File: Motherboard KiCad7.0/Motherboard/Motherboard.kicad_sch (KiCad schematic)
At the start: 92 parts, among them J1 USB_B_Micro, J10 430450200, J11 430450200, J12 430450200, J2 SWD_01x04_Pin, J3 430450200, J4 430450200, J5 B04B-XASK-1, J6 430450200, J7 430450200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

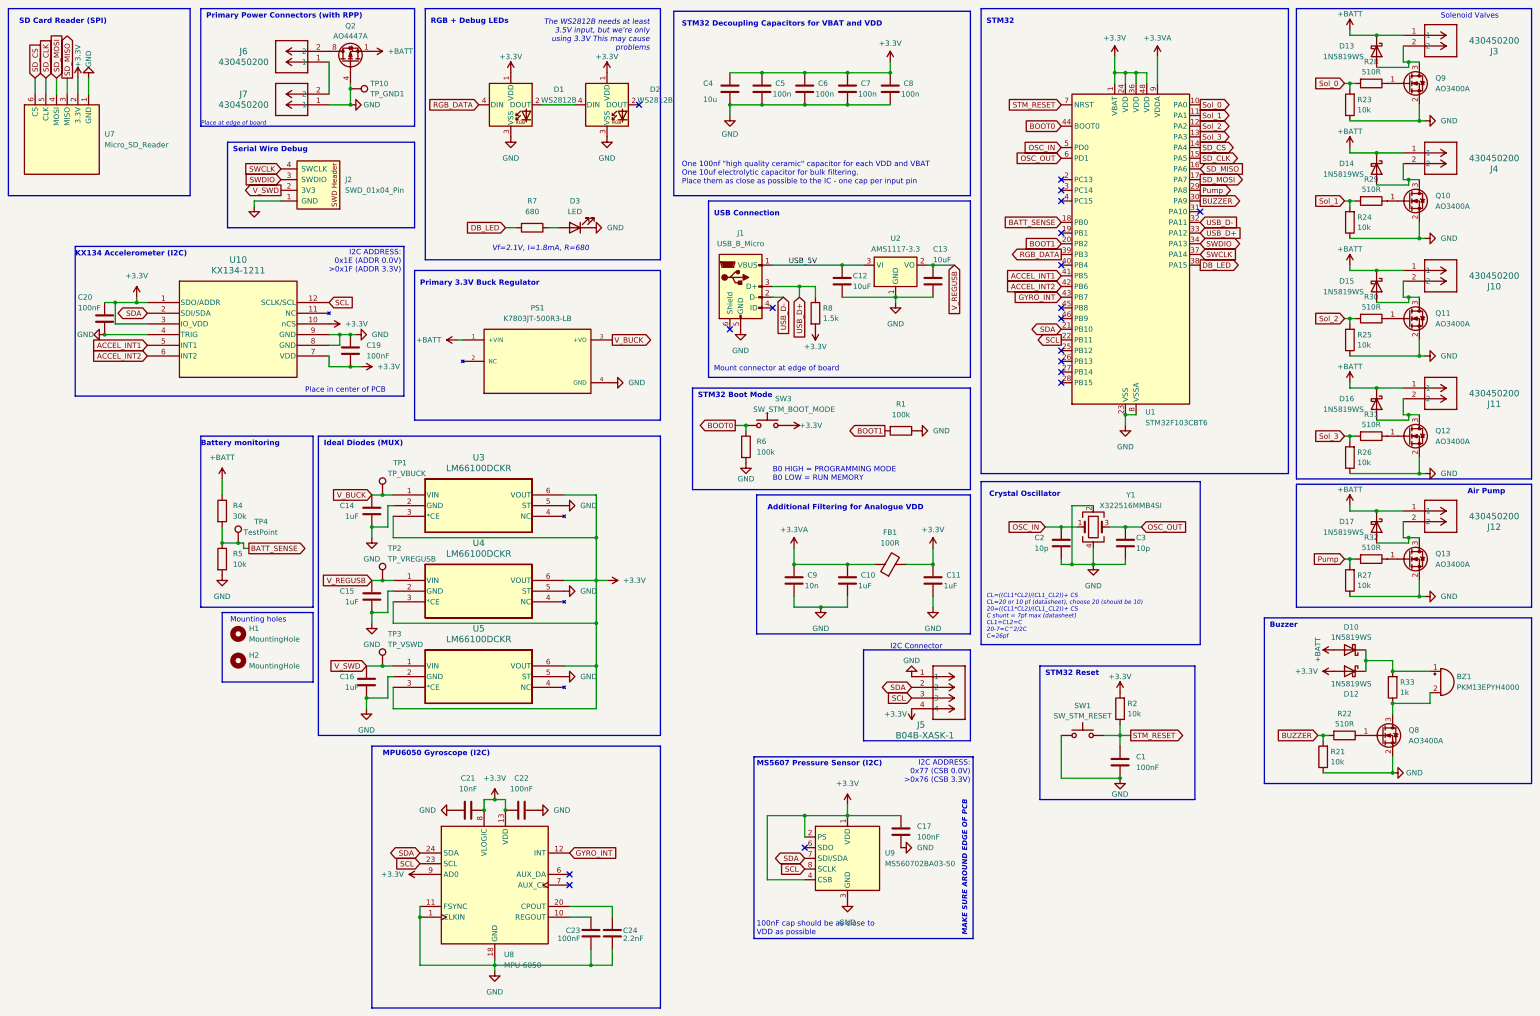
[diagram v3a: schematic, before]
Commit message: Schematic and layout changes
Rewired ADCs
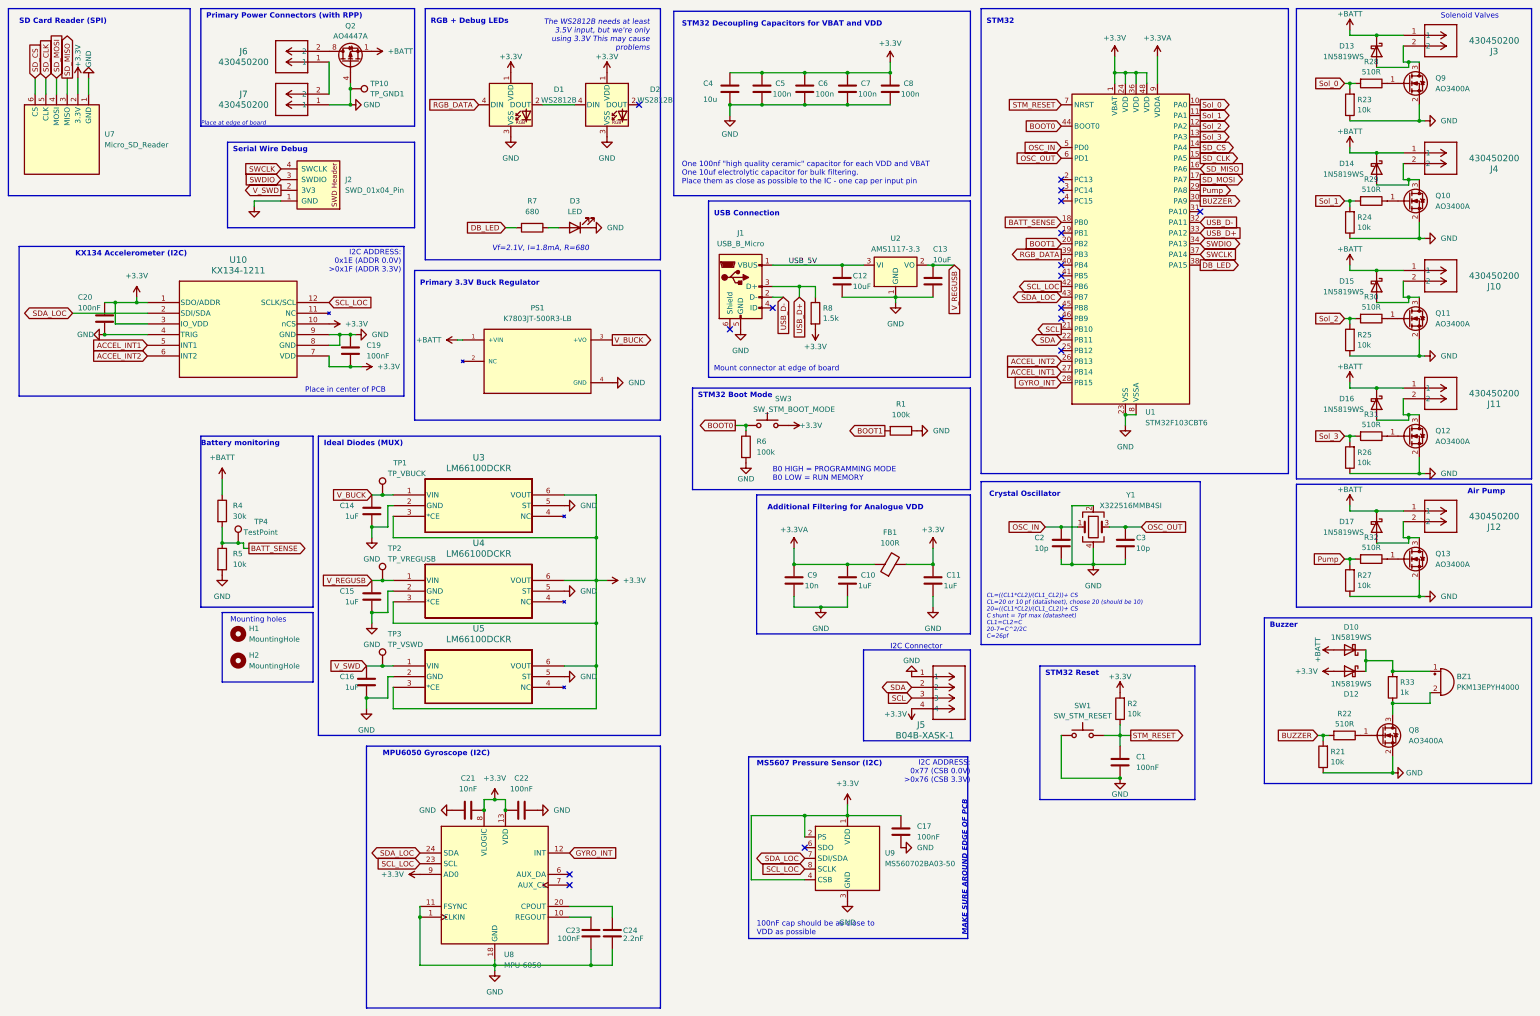
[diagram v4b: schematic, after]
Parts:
- J10, J11, J12, J4, J6, J7: footprint CON_430450200_MOL -> CONN 0430450200:CON_430450200_MOL
- J5: footprint CONN_B04B-XASK-1_JST -> B04B_XASK_1:CONN_B04B-XASK-1_JST
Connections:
- net ACCEL_INT1: now also U1.27 (PB14); no longer U1.41 (PB5)
- net ACCEL_INT2: now also U1.26 (PB13); no longer U1.42 (PB6)
- net GYRO_INT: now also U1.28 (PB15); no longer U1.43 (PB7)
- net SCL: now also U1.21 (PB10); no longer U1.22 (PB11), U10.12 (SCLK/SCL), U8.23 (SCL), U9.8 (SCLK)
- net SDA: now also U1.22 (PB11); no longer U1.21 (PB10), U10.2 (SDI/SDA), U8.24 (SDA), U9.7 (SDI/SDA)
- new net SCL_LOC: U1.42 (PB6), U10.12 (SCLK/SCL), U8.23 (SCL), U9.8 (SCLK)
- new net SDA_LOC: U1.43 (PB7), U10.2 (SDI/SDA), U8.24 (SDA), U9.7 (SDI/SDA)
- no-connect marks 18 -> 16
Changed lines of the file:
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@@
   (junction (at 388.62 71.12) (diameter 0) (color 0 0 0 0)
   )
-  (no_connect (at 303.53 102.87))
-  (no_connect (at 303.53 100.33))
   (no_connect (at 303.53 90.17))
   (no_connect (at 203.2 39.37))
   (no_connect (at 303.53 62.23))
   (no_connect (at 303.53 87.63))
+  (no_connect (at 303.53 80.01))
   (no_connect (at 303.53 77.47))
-  (no_connect (at 303.53 105.41))
   (no_connect (at 234.95 87.63))
   (no_connect (at 336.55 64.77))
@@
     (stroke (width 0) (type default))
   )
-  (wire (pts (xy 233.68 223.52) (xy 233.68 208.28))
+  (wire (pts (xy 229.87 223.52) (xy 229.87 208.28))
     (stroke (width 0) (type default))
   )
@@
     (stroke (width 0) (type default))
   )
-  (wire (pts (xy 233.68 208.28) (xy 242.57 208.28))
+  (wire (pts (xy 229.87 208.28) (xy 242.57 208.28))
     (stroke (width 0) (type default))
   )
@@
     (stroke (width 0) (type default))
   )
-  (wire (pts (xy 242.57 223.52) (xy 233.68 223.52))
+  (wire (pts (xy 242.57 223.52) (xy 229.87 223.52))
     (stroke (width 0) (type default))
   )
@@
     (stroke (width 0) (type default))
   )
+  (wire (pts (xy 68.58 88.9) (xy 86.36 88.9))
+    (stroke (width 0) (type default))
+  )
   (wire (pts (xy 372.11 106.68) (xy 378.46 106.68))
     (stroke (width 0) (type default))
@@
     (fill (type none))
   )
-  (rectangle (start 230.505 194.31) (end 282.575 237.49)
+  (rectangle (start 229.235 194.31) (end 281.305 237.49)
     (stroke (width 0) (type default))
     (fill (type none))
@@
     (fill (type none))
   )
-  (rectangle (start 69.215 73.025) (end 147.32 108.585)
+  (rectangle (start 55.88 73.025) (end 147.32 108.585)
     (stroke (width 0) (type default))
     (fill (type none))
@@
     (fill (type none))
   )
-  (rectangle (start 139.7 191.77) (end 208.28 254)
+  (rectangle (start 138.43 191.77) (end 208.28 254)
     (stroke (width 0) (type default))
     (fill (type none))
@@
     (effects (font (size 1.27 1.27)) (justify left bottom))
   )
+  (global_label "SCL_LOC" (shape output) (at 303.53 82.55 180) (fields_autoplaced)
+    (effects (font (size 1.27 1.27)) (justify right))
+    (property "Intersheetrefs" "${INTERSHEET_REFS}" (at 292.441 82.55 0)
+      (effects (font (size 1.27 1.27)) (justify right) hide)
+    )
+  )
   (global_label "SWDIO" (shape bidirectional) (at 336.55 72.39 0) (fields_autoplaced)
     (effects (font (size 1.27 1.27)) (justify left))
@@
     )
   )
-  (global_label "SDA" (shape bidirectional) (at 151.13 217.17 180) (fields_autoplaced)
+  (global_label "SDA_LOC" (shape bidirectional) (at 151.13 217.17 180) (fields_autoplaced)
     (effects (font (size 1.27 1.27)) (justify right))
-    (property "Intersheetrefs" "${INTERSHEET_REFS}" (at 143.4654 217.17 0)
+    (property "Intersheetrefs" "${INTERSHEET_REFS}" (at 138.8692 217.17 0)
       (effects (font (size 1.27 1.27)) (justify right) hide)
     )
@@
     )
   )
-  (global_label "SCL" (shape output) (at 303.53 95.25 180) (fields_autoplaced)
+  (global_label "SCL" (shape output) (at 303.53 92.71 180) (fields_autoplaced)
     (effects (font (size 1.27 1.27)) (justify right))
-    (property "Intersheetrefs" "${INTERSHEET_REFS}" (at 297.0372 95.25 0)
+    (property "Intersheetrefs" "${INTERSHEET_REFS}" (at 297.0372 92.71 0)
       (effects (font (size 1.27 1.27)) (justify right) hide)
     )
@@
     )
   )
-  (global_label "SCL" (shape input) (at 242.57 220.98 180) (fields_autoplaced)
+  (global_label "SCL_LOC" (shape input) (at 242.57 220.98 180) (fields_autoplaced)
     (effects (font (size 1.27 1.27)) (justify right))
-    (property "Intersheetrefs" "${INTERSHEET_REFS}" (at 236.0772 220.98 0)
+    (property "Intersheetrefs" "${INTERSHEET_REFS}" (at 231.481 220.98 0)
       (effects (font (size 1.27 1.27)) (justify right) hide)
     )
@@
     )
   )
-  (global_label "SDA" (shape bidirectional) (at 86.36 88.9 180) (fields_autoplaced)
+  (global_label "SDA_LOC" (shape bidirectional) (at 68.58 88.9 180) (fields_autoplaced)
     (effects (font (size 1.27 1.27)) (justify right))
-    (property "Intersheetrefs" "${INTERSHEET_REFS}" (at 78.6954 88.9 0)
+    (property "Intersheetrefs" "${INTERSHEET_REFS}" (at 56.3192 88.9 0)
       (effects (font (size 1.27 1.27)) (justify right) hide)
     )
   )
-  (global_label "SCL" (shape input) (at 151.13 219.71 180) (fields_autoplaced)
+  (global_label "SCL_LOC" (shape input) (at 151.13 219.71 180) (fields_autoplaced)
     (effects (font (size 1.27 1.27)) (justify right))
-    (property "Intersheetrefs" "${INTERSHEET_REFS}" (at 144.6372 219.71 0)
+    (property "Intersheetrefs" "${INTERSHEET_REFS}" (at 140.041 219.71 0)
       (effects (font (size 1.27 1.27)) (justify right) hide)
     )
   )
-  (global_label "ACCEL_INT1" (shape input) (at 303.53 80.01 180) (fields_autoplaced)
+  (global_label "ACCEL_INT1" (shape input) (at 303.53 102.87 180) (fields_autoplaced)
     (effects (font (size 1.27 1.27)) (justify right))
-    (property "Intersheetrefs" "${INTERSHEET_REFS}" (at 289.6591 80.01 0)
+    (property "Intersheetrefs" "${INTERSHEET_REFS}" (at 289.6591 102.87 0)
       (effects (font (size 1.27 1.27)) (justify right) hide)
     )
@@
     )
   )
+  (global_label "SDA_LOC" (shape bidirectional) (at 303.53 85.09 180) (fields_autoplaced)
+    (effects (font (size 1.27 1.27)) (justify right))
+    (property "Intersheetrefs" "${INTERSHEET_REFS}" (at 291.2692 85.09 0)
+      (effects (font (size 1.27 1.27)) (justify right) hide)
+    )
+  )
   (global_label "BOOT1" (shape output) (at 261.62 116.84 180) (fields_autoplaced)
     (effects (font (size 1.27 1.27)) (justify right))
@@
     )
   )
-  (global_label "ACCEL_INT2" (shape input) (at 303.53 82.55 180) (fields_autoplaced)
+  (global_label "ACCEL_INT2" (shape input) (at 303.53 100.33 180) (fields_autoplaced)
     (effects (font (size 1.27 1.27)) (justify right))
-    (property "Intersheetrefs" "${INTERSHEET_REFS}" (at 289.6591 82.55 0)
+    (property "Intersheetrefs" "${INTERSHEET_REFS}" (at 289.6591 100.33 0)
       (effects (font (size 1.27 1.27)) (justify right) hide)
     )
@@
     )
   )
-  (global_label "SDA" (shape bidirectional) (at 242.57 218.44 180) (fields_autoplaced)
+  (global_label "SDA_LOC" (shape bidirectional) (at 242.57 218.44 180) (fields_autoplaced)
     (effects (font (size 1.27 1.27)) (justify right))
-    (property "Intersheetrefs" "${INTERSHEET_REFS}" (at 234.9054 218.44 0)
+    (property "Intersheetrefs" "${INTERSHEET_REFS}" (at 230.3092 218.44 0)
       (effects (font (size 1.27 1.27)) (justify right) hide)
     )
@@
     )
   )
-  (global_label "SDA" (shape bidirectional) (at 303.53 92.71 180) (fields_autoplaced)
+  (global_label "SDA" (shape bidirectional) (at 303.53 95.25 180) (fields_autoplaced)
     (effects (font (size 1.27 1.27)) (justify right))
-    (property "Intersheetrefs" "${INTERSHEET_REFS}" (at 295.8654 92.71 0)
+    (property "Intersheetrefs" "${INTERSHEET_REFS}" (at 295.8654 95.25 0)
       (effects (font (size 1.27 1.27)) (justify right) hide)
     )
   )
-  (global_label "GYRO_INT" (shape input) (at 303.53 85.09 180) (fields_autoplaced)
+  (global_label "GYRO_INT" (shape input) (at 303.53 105.41 180) (fields_autoplaced)
     (effects (font (size 1.27 1.27)) (justify right))
-    (property "Intersheetrefs" "${INTERSHEET_REFS}" (at 291.7152 85.09 0)
+    (property "Intersheetrefs" "${INTERSHEET_REFS}" (at 291.7152 105.41 0)
       (effects (font (size 1.27 1.27)) (justify right) hide)
     )
@@
     )
   )
-  (global_label "SCL" (shape input) (at 129.54 86.36 0) (fields_autoplaced)
+  (global_label "SCL_LOC" (shape input) (at 129.54 86.36 0) (fields_autoplaced)
     (effects (font (size 1.27 1.27)) (justify left))
-    (property "Intersheetrefs" "${INTERSHEET_REFS}" (at 136.0328 86.36 0)
+    (property "Intersheetrefs" "${INTERSHEET_REFS}" (at 140.629 86.36 0)
       (effects (font (size 1.27 1.27)) (justify left) hide)
     )
@@
       (effects (font (size 1.524 1.524)))
     )
-    (property "Footprint" "CON_430450200_MOL" (at 133.35 33.02 0)
+    (property "Footprint" "CONN 0430450200:CON_430450200_MOL" (at 133.35 33.02 0)
       (effects (font (size 1.27 1.27) italic) hide)
     )
@@
       (effects (font (size 1.524 1.524)))
     )
-    (property "Footprint" "CON_430450200_MOL" (at 381 132.08 0)
+    (property "Footprint" "CONN 0430450200:CON_430450200_MOL" (at 381 132.08 0)
       (effects (font (size 1.27 1.27) italic) hide)
     )
@@
       (effects (font (size 1.524 1.524)))
     )
-    (property "Footprint" "CON_430450200_MOL" (at 381 102.87 0)
+    (property "Footprint" "CONN 0430450200:CON_430450200_MOL" (at 381 102.87 0)
       (effects (font (size 1.27 1.27) italic) hide)
     )
@@
       (effects (font (size 1.524 1.524)))
     )
-    (property "Footprint" "CON_430450200_MOL" (at 133.35 43.18 0)
+    (property "Footprint" "CONN 0430450200:CON_430450200_MOL" (at 133.35 43.18 0)
       (effects (font (size 1.27 1.27) italic) hide)
     )
@@
       (effects (font (size 1.524 1.524)))
     )
-    (property "Footprint" "CON_430450200_MOL" (at 381 46.99 0)
+    (property "Footprint" "CONN 0430450200:CON_430450200_MOL" (at 381 46.99 0)
       (effects (font (size 1.27 1.27) italic) hide)
     )
@@
       (effects (font (size 1.524 1.524)))
     )
-    (property "Footprint" "CON_430450200_MOL" (at 381 74.93 0)
+    (property "Footprint" "CONN 0430450200:CON_430450200_MOL" (at 381 74.93 0)
       (effects (font (size 1.27 1.27) italic) hide)
     )
@@
       (effects (font (size 1.524 1.524)) (justify left))
     )
-    (property "Footprint" "CONN_B04B-XASK-1_JST" (at 267.97 167.64 0)
+    (property "Footprint" "B04B_XASK_1:CONN_B04B-XASK-1_JST" (at 267.97 167.64 0)
       (effects (font (size 1.27 1.27) italic) hide)
     )
